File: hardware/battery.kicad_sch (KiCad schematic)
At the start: 34 parts, among them J2 B2B-XH-A, J3 PRPC001DAAN-RC, Q1 DMG2305UX-7, Q2 DMN2005, Q3 DMN2005, U2 BQ29728DSER, U3 MCP73833T-FCI/MF

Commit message: HW: Improve comments
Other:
- note added: "A 1S 3.7V nominal LiPo battery can be used to power the device. When powered by the battery, the device typically consumes between 10 mA (in sleep mode) and 700 mA (during data transmission). The charging current is 450 mA, so connect a battery with a capacity of at least 450 mAh. When powered via USB-C, the battery can be charged."
- note added: "To ensure compatibility with a wide range of LiPo batteries, set the charging current to 450 mA. To visually confirm that charging is in progress and that the battery is being utilized, LEDs will indicate the status according to the "STATUS OUTPUTS" table."
- note added: "To ensure safety when handling LiPo batteries, it is essential to protect against the following risks: - Overcurrent during charging - Overcurrent during discharging - Overvoltage - Undervoltage - Reverse polarity - Short circuits"
- note removed: "A 3.7 V nominal LiPo battery can be used to power the device. The device nominally consumes from 10 mA (sleep) to 700 mA (data transmit) when battery powered. The charging current is 450 mA, so connect a battery with ≥ 450 mAh capacity. When powered by the USB-C, the battery can be charged."
- note removed: "As LiPo batteries can be dangerous, ensure that we are protected against: - Over-current charge - Over-current discharge - Over-voltage - Under-voltage - Reverse polarity - Short circuit"
- note removed: "To ensure support for a wide variety of LiPo batteries, set the charging current to 450 mA. To visually confirm that charging is happening and that the battery is being used, LEDs are used according to the "STATUS OUTPUTS" table."
- moved on the sheet: C3, C4, F2, J3, Q1, Q2, Q3, R3, R4, R5, TP4, TP5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

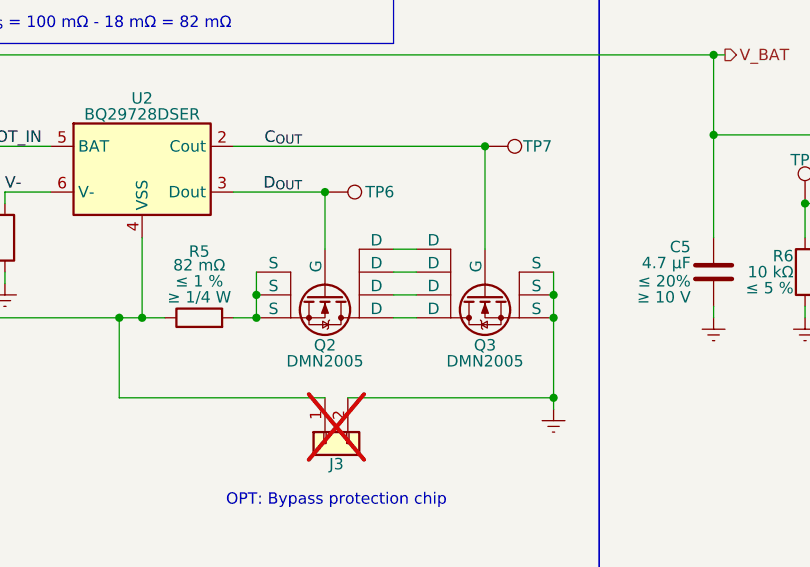
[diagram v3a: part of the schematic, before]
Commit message: HW: Connect BAT_PROT drains together
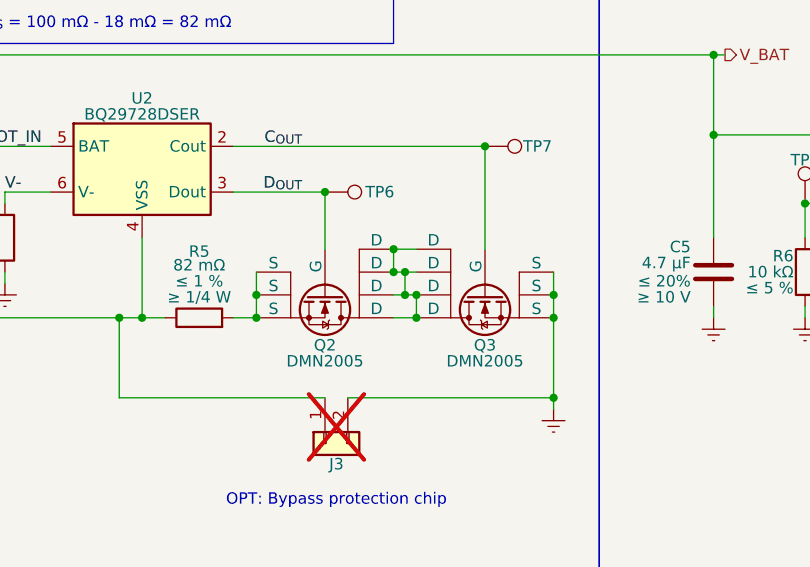
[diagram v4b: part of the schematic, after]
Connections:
- net at Q2.5 (D), Q3.5 (D): now also Q2.6 (D), Q2.7 (D), Q2.8 (D), Q3.6 (D), Q3.7 (D), Q3.8 (D)
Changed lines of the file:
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@@
 	(title_block
 		(title "Iida devkit")
-		(date "2025-05-12")
+		(date "2025-05-13")
 		(rev "v5.0.0")
 	)
@@
 	)
 	(junction
+		(at 220.98 166.37)
+		(diameter 0)
+		(color 0 0 0 0)
+	)
+	(junction
 		(at 124.46 168.91)
 		(diameter 0)
@@
 	)
 	(junction
+		(at 218.44 163.83)
+		(diameter 0)
+		(color 0 0 0 0)
+	)
+	(junction
+		(at 220.98 168.91)
+		(diameter 0)
+		(color 0 0 0 0)
+	)
+	(junction
 		(at 203.2 166.37)
 		(diameter 0)
@@
 	)
 	(junction
+		(at 219.71 166.37)
+		(diameter 0)
+		(color 0 0 0 0)
+	)
+	(junction
 		(at 162.56 149.86)
 		(diameter 0)
@@
 	)
 	(junction
+		(at 218.44 161.29)
+		(diameter 0)
+		(color 0 0 0 0)
+	)
+	(junction
 		(at 144.78 149.86)
 		(diameter 0)
 		(color 0 0 0 0)
 	)
+	(junction
+		(at 219.71 163.83)
+		(diameter 0)
+		(color 0 0 0 0)
+	)
 	(wire
 		(pts
@@
 	(wire
 		(pts
-			(xy 218.44 166.37) (xy 220.98 166.37)
+			(xy 218.44 166.37) (xy 219.71 166.37)
+		)
+		(stroke
+			(width 0)
+			(type default)
+		)
+	)
+	(wire
+		(pts
+			(xy 219.71 166.37) (xy 220.98 166.37)
 		)
 		(stroke
@@
 	(wire
 		(pts
+			(xy 218.44 161.29) (xy 218.44 163.83)
+		)
+		(stroke
+			(width 0)
+			(type default)
+		)
+	)
+	(wire
+		(pts
 			(xy 254 139.7) (xy 152.4 139.7)
 		)
@@
 	(wire
 		(pts
+			(xy 219.71 163.83) (xy 219.71 166.37)
+		)
+		(stroke
+			(width 0)
+			(type default)
+		)
+	)
+	(wire
+		(pts
 			(xy 269.24 158.75) (xy 280.67 158.75)
 		)
@@
 	(wire
 		(pts
+			(xy 219.71 163.83) (xy 220.98 163.83)
+		)
+		(stroke
+			(width 0)
+			(type default)
+		)
+	)
+	(wire
+		(pts
 			(xy 294.64 165.1) (xy 294.64 163.83)
 		)
@@
 	(wire
 		(pts
+			(xy 220.98 166.37) (xy 220.98 168.91)
+		)
+		(stroke
+			(width 0)
+			(type default)
+		)
+	)
+	(wire
+		(pts
 			(xy 162.56 163.83) (xy 162.56 168.91)
 		)
@@
 	(wire
 		(pts
-			(xy 218.44 163.83) (xy 220.98 163.83)
-		)
-		(stroke
+			(xy 218.44 163.83) (xy 219.71 163.83)
+		)
+		(stroke

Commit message: HW: Add battery monitoring with MAX17048
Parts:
- added C7: 0.1 µF, Capacitor_SMD:C_0402_1005Metric, symbol Device:C
- added TP13: TestPoint, TestPoint:TestPoint_Pad_D1.0mm, symbol Connector:TestPoint
- added U4: MAX17048, Package_DFN_QFN:TDFN-8-1EP_2x2mm_P0.5mm_EP0.8x1.2mm, symbol MAX17048:MAX17048
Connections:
- net GND: now also C7.2, U4.1 (CTG), U4.4 (GND), U4.6 (QSTRT), U4.9 (EP)
- net V_BAT: now also C7.1, U4.2 (CELL), U4.3 (V_{DD})
- new net BAT_INT: TP13.1, U4.5 (~{ALRT})
- new net I2C_SCL: U4.7 (SCL)
- new net I2C_SDA: U4.8 (SDA)
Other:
- note removed: "A 1S 3.7V nominal LiPo battery can be used to power the device. When powered by the battery, the device typically consumes between 10 mA (in sleep mode) and 700 mA (during data transmission). The charging current is 450 mA, so connect a battery with a capacity of at least 450 mAh. When powered via USB-C, the battery can be charged."
- note removed: "To ensure compatibility with a wide range of LiPo batteries, set the charging current to 450 mA. To visually confirm that charging is in progress and that the battery is being utilized, LEDs will indicate the status according to the "STATUS OUTPUTS" table."
- note removed: "To ensure safety when handling LiPo batteries, it is essential to protect against the following risks: - Overcurrent during charging - Overcurrent during discharging - Overvoltage - Undervoltage - Reverse polarity - Short circuits"
- moved on the sheet: C3, C4, C5, C6, F2, J2, J3, LED1, LED2, LED3, Q1, Q2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

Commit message: HW: Reorganize schematic
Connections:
- net BAT_INT renamed BAT_INTn
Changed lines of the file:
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@@
 		)
 	)
-	(hierarchical_label "BAT_INT"
+	(hierarchical_label "BAT_INTn"
 		(shape output)
 		(at 381 181.61 0)

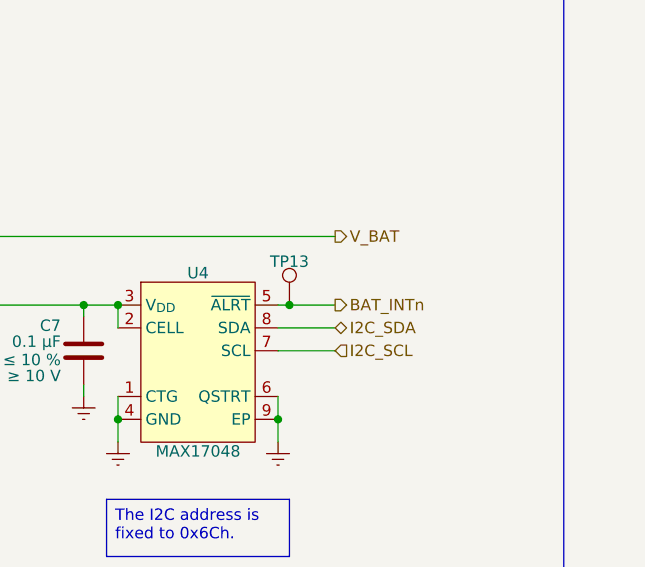
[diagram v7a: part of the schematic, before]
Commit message: HW: Add humidity sensor
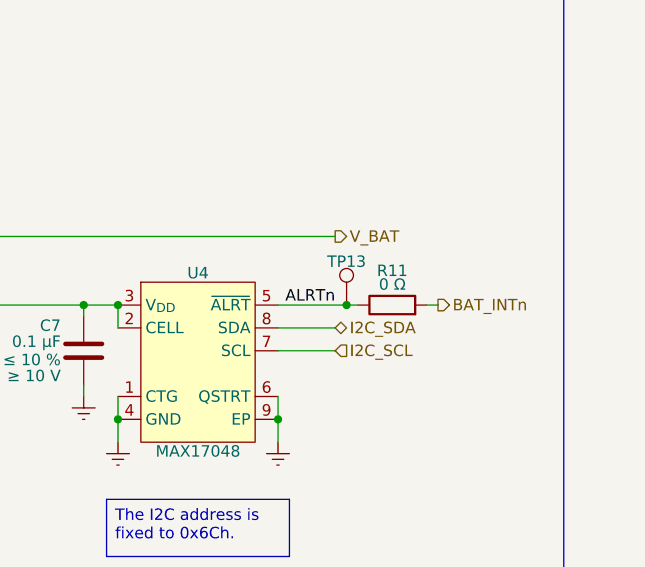
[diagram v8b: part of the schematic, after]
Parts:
- added R11: 0 Ω, Resistor_SMD:R_0402_1005Metric, symbol Device:R
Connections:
- net BAT_INTn: now also R11.2; no longer TP13.1, U4.5 (~{ALRT})
- new net ALRTn: R11.1, TP13.1, U4.5 (~{ALRT})
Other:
- moved on the sheet: TP13
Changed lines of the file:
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@@
 	(title_block
 		(title "Iida devkit")
-		(date "2025-05-13")
+		(date "2025-05-14")
 		(rev "v5.0.0")
 	)
@@
 	)
 	(junction
-		(at 39.37 199.39)
+		(at 382.27 181.61)
 		(diameter 0)
 		(color 0 0 0 0)
 	)
 	(junction
-		(at 125.73 191.77)
+		(at 39.37 199.39)
 		(diameter 0)
 		(color 0 0 0 0)
 	)
 	(junction
-		(at 375.92 181.61)
+		(at 125.73 191.77)
 		(diameter 0)
 		(color 0 0 0 0)
@@
 	(wire
 		(pts
+			(xy 382.27 181.61) (xy 383.54 181.61)
+		)
+		(stroke
+			(width 0)
+			(type default)
+		)
+	)
+	(wire
+		(pts
 			(xy 353.06 181.61) (xy 353.06 182.88)
 		)
@@
 	(wire
 		(pts
+			(xy 391.16 181.61) (xy 392.43 181.61)
+		)
+		(stroke
+			(width 0)
+			(type default)
+		)
+	)
+	(wire
+		(pts
 			(xy 124.46 191.77) (xy 125.73 191.77)
 		)
@@
 	(wire
 		(pts
-			(xy 374.65 181.61) (xy 375.92 181.61)
+			(xy 374.65 181.61) (xy 382.27 181.61)
 		)
 		(stroke
@@
 	(wire
 		(pts
-			(xy 375.92 181.61) (xy 381 181.61)
-		)
-		(stroke
-			(width 0)
-			(type default)
-		)
-	)
-	(wire
-		(pts
 			(xy 172.72 205.74) (xy 173.99 205.74)
 		)
@@
 		)
 	)
+	(label "ALRTn"
+		(at 381 181.61 180)
+		(effects
+			(font
+				(size 1.27 1.27)
+			)
+			(justify right bottom)
+		)
+	)
 	(label "BATT+"
 		(at 38.1 199.39 180)
@@
 	(hierarchical_label "BAT_INTn"
 		(shape output)
-		(at 381 181.61 0)
+		(at 392.43 181.61 0)
 		(effects
 			(font
@@
 	)
 	(symbol
+		(lib_id "Device:R")
+		(at 387.35 181.61 90)
+		(unit 1)
+		(exclude_from_sim no)
+		(in_bom yes)
+		(on_board yes)
+		(dnp no)
+		(property "Reference" "R11"
+			(at 387.35 177.8 90)
+			(effects
+				(font
+					(size 1.27 1.27)
+				)
+			)
+		)
+		(property "Value" "0 Ω"
+			(at 387.35 179.324 90)
+			(effects
+				(font
+					(size 1.27 1.27)
+				)
+			)
+		)
+		(property "Footprint" "Resistor_SMD:R_0402_1005Metric"
+			(at 387.35 183.388 90)
+			(effects
+				(font
+					(size 1.27 1.27)
+				)
+				(hide yes)
+			)
+		)
+		(property "Datasheet" "~"
+			(at 387.35 181.61 0)
+			(effects
+				(font
+					(size 1.27 1.27)
+				)
+				(hide yes)
+			)
+		)
+		(property "Description" ""
+			(at 387.35 181.61 0)
+			(effects
+				(font
+					(size 1.27 1.27)
+				)
+				(hide yes)
+			)
+		)
+		(property "Manufacturer" "Würth Elektronik"
+			(at 387.35 181.61 0)
+			(effects
+				(font
+					(size 1.27 1.27)
+				)
+				(hide yes)
+			)
+		)
+		(property "Footprint review check" "+"
+			(at 387.35 181.61 0)
+			(effects
+				(font
+					(size 1.27 1.27)
+				)
+				(hide yes)
+			)
+		)
+		(property "MPN" "560112110001"
+			(at 387.35 181.61 0)
+			(effects
+				(font
+					(size 1.27 1.27)
+				)
+				(hide yes)
+			)
+		)
+		(property "Size" "0402"
+			(at 387.35 181.61 0)
+			(effects
+				(font
+					(size 1.27 1.27)
+				)
+				(hide yes)
+			)
+		)
+		(property "DigiKey Part Number" "732-560112110001CT-ND"
+			(at 387.35 181.61 90)
+			(effects
+				(font
+					(size 1.27 1.27)
+				)
+				(hide yes)
+			)
+		)
+		(property "Power" ""
+			(at 387.35 181.61 90)
+			(effects
+				(font
+					(size 1.27 1.27)
+				)
+				(hide yes)
+			)
+		)
+		(pin "2"
+		)
+		(pin "1"
+		)
+		(instances
+			(project "iida_devkit"
+				(path "/b12a6e25-97fb-4aba-bc96-af8db389bb9a/87c570c0-3d52-431f-af75-588e9bdc1a2a"
+					(reference "R11")
+					(unit 1)
+				)
+			)
+		)
+	)
+	(symbol
 		(lib_id "Connector:TestPoint")
 		(at 290.83 201.93 90)
@@
 	(symbol
 		(lib_id "Connector:TestPoint")
-		(at 375.92 181.61 0)
+		(at 382.27 181.61 0)
 		(unit 1)
 		(exclude_from_sim no)
@@
 		(dnp no)
 		(property "Reference" "TP13"
-			(at 375.92 176.784 0)
+			(at 382.27 176.784 0)
 			(effects
 				(font
@@
 		)
 		(property "Value" "TestPoint"
-			(at 378.46 179.5779 0)
+			(at 384.81 179.5779 0)
 			(effects
 				(font
@@
 		)
 		(property "Footprint" "TestPoint:TestPoint_Pad_D1.0mm"
-			(at 381 181.61 0)
+			(at 387.35 181.61 0)
 			(effects
 				(font
@@
 		)
 		(property "Datasheet" "~"
-			(at 381 181.61 0)
+			(at 387.35 181.61 0)
 			(effects
 				(font
@@
 		)
 		(property "Description" "test point"
-			(at 375.92 181.61 0)
+			(at 382.27 181.61 0)
 			(effects
 				(font
